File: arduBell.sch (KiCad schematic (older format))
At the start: 20 parts, among them J1 AVR-ISP-6, J2 UART, J3 VCC, J4 BELL, J5 RELAY1, J6 RELAY2, U1 ATMEGA328P-AU, U2 NSL-32, Y1 Crystal_GND2

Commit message: rev 1a, XO fixed, more labels and rearranging
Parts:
- removed Y1: Crystal_GND2, Crystal:Crystal_HC49-4H_Vertical, symbol Device:Crystal_GND2
- added C10, C9: 10p, Capacitor_SMD:C_0603_1608Metric, symbol Device:C_Small
- added Y1: Crystal, symbol Device:Crystal
- C1, C2, C5: value C_Small -> 100n
- C3: value C_Small -> 1u
- C4, C6: value CP_Small -> 4.7u
- J2: symbol dk_Rectangular-Connectors-Headers-Male-Pins:640456-3 -> arduBell-rescue:640456-3-dk_Rectangular-Connectors-Headers-Male-Pins
- J3, J4, J5, J6: symbol dk_Rectangular-Connectors-Headers-Male-Pins:22-23-2021 -> arduBell-rescue:22-23-2021-dk_Rectangular-Connectors-Headers-Male-Pins
- R1, R2, R3: value R_Small -> 1K
- S1: symbol dk_Pushbutton-Switches:GPTS203211B -> arduBell-rescue:GPTS203211B-dk_Pushbutton-Switches
- U1: symbol dk_Embedded-Microcontrollers:ATMEGA328P-AU -> arduBell-rescue:ATMEGA328P-AU-dk_Embedded-Microcontrollers
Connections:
- net GND: now also C10.2, C9.2
- net at U1.7 (PB6): now also C9.1, Y1.1
- net at U1.8 (PB7): now also C10.1, Y1.2
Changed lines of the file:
@@
 $EndDescr
 $Comp
-L dk_Embedded-Microcontrollers:ATMEGA328P-AU U1
+L arduBell-rescue:ATMEGA328P-AU-dk_Embedded-Microcontrollers U1
 U 1 1 5FF53399
 P 5900 3950
@@
 $EndComp
 $Comp
-L dk_Rectangular-Connectors-Headers-Male-Pins:22-23-2021 J3
+L arduBell-rescue:22-23-2021-dk_Rectangular-Connectors-Headers-Male-Pins J3
 U 1 1 5FF54EE3
 P 6750 1700
@@
 P 6050 1250
 F 0 "C2" V 5821 1250 50  0000 C CNN
-F 1 "C_Small" V 5912 1250 50  0000 C CNN
+F 1 "100n" V 5912 1250 50  0000 C CNN
 F 2 "Capacitor_SMD:C_0603_1608Metric" H 6050 1250 50  0001 C CNN
 F 3 "~" H 6050 1250 50  0001 C CNN
@@
 P 6050 1600
 F 0 "C3" V 5821 1600 50  0000 C CNN
-F 1 "C_Small" V 5912 1600 50  0000 C CNN
+F 1 "1u" V 5912 1600 50  0000 C CNN
 F 2 "Capacitor_SMD:C_0603_1608Metric" H 6050 1600 50  0001 C CNN
 F 3 "~" H 6050 1600 50  0001 C CNN
@@
 P 6050 1950
 F 0 "C4" V 5825 1950 50  0000 C CNN
-F 1 "CP_Small" V 5916 1950 50  0000 C CNN
+F 1 "4.7u" V 5916 1950 50  0000 C CNN
 F 2 "Capacitor_SMD:C_1206_3216Metric" H 6050 1950 50  0001 C CNN
 F 3 "~" H 6050 1950 50  0001 C CNN
@@
 Wire Wire Line
 	6600 1700 6650 1700
-$Comp
-L Device:Crystal_GND2 Y1
-U 1 1 5FF6D2C8
-P 4400 2900
-F 0 "Y1" V 4354 3030 50  0000 L CNN
-F 1 "Crystal_GND2" V 4445 3030 50  0000 L CNN
-F 2 "Crystal:Crystal_HC49-4H_Vertical" H 4400 2900 50  0001 C CNN
-F 3 "~" H 4400 2900 50  0001 C CNN
-	1    4400 2900
-	0    1    1    0
-$EndComp
 Wire Wire Line
 	4400 2750 5200 2750
@@
 L power:GND #PWR0105
 U 1 1 5FF6EA88
-P 4100 3000
-F 0 "#PWR0105" H 4100 2750 50  0001 C CNN
-F 1 "GND" H 4105 2827 50  0000 C CNN
-F 2 "" H 4100 3000 50  0001 C CNN
-F 3 "" H 4100 3000 50  0001 C CNN
-	1    4100 3000
-	1    0    0    -1
-$EndComp
-Wire Wire Line
-	4100 3000 4100 2900
-Wire Wire Line
-	4100 2900 4200 2900
+P 3950 2950
+F 0 "#PWR0105" H 3950 2700 50  0001 C CNN
+F 1 "GND" H 3955 2777 50  0000 C CNN
+F 2 "" H 3950 2950 50  0001 C CNN
+F 3 "" H 3950 2950 50  0001 C CNN
+	1    3950 2950
+	1    0    0    -1
+$EndComp
 $Comp
 L Device:C_Small C1
@@
 P 4600 5050
 F 0 "C1" V 4371 5050 50  0000 C CNN
-F 1 "C_Small" V 4462 5050 50  0000 C CNN
+F 1 "100n" V 4462 5050 50  0000 C CNN
 F 2 "Capacitor_SMD:C_0603_1608Metric" H 4600 5050 50  0001 C CNN
 F 3 "~" H 4600 5050 50  0001 C CNN
@@
 P 3850 4750
 F 0 "R2" V 4046 4750 50  0000 C CNN
-F 1 "R_Small" V 3955 4750 50  0000 C CNN
+F 1 "1K" V 3955 4750 50  0000 C CNN
 F 2 "Resistor_SMD:R_0603_1608Metric" H 3850 4750 50  0001 C CNN
 F 3 "~" H 3850 4750 50  0001 C CNN
@@
 P 4150 4650
 F 0 "R3" V 4346 4650 50  0000 C CNN
-F 1 "R_Small" V 4255 4650 50  0000 C CNN
+F 1 "1K" V 4255 4650 50  0000 C CNN
 F 2 "Resistor_SMD:R_0603_1608Metric" H 4150 4650 50  0001 C CNN
 F 3 "~" H 4150 4650 50  0001 C CNN
@@
 	5400 4550 4950 4550
 $Comp
-L dk_Pushbutton-Switches:GPTS203211B S1
+L arduBell-rescue:GPTS203211B-dk_Pushbutton-Switches S1
 U 1 1 5FF7A8EF
 P 1700 4500
@@
 P 1900 3950
 F 0 "R1" H 1959 3996 50  0000 L CNN
-F 1 "R_Small" H 1959 3905 50  0000 L CNN
+F 1 "1K" H 1959 3905 50  0000 L CNN
 F 2 "Resistor_SMD:R_0603_1608Metric" H 1900 3950 50  0001 C CNN
 F 3 "~" H 1900 3950 50  0001 C CNN
@@
 $EndComp
 $Comp
-L dk_Rectangular-Connectors-Headers-Male-Pins:22-23-2021 J4
+L arduBell-rescue:22-23-2021-dk_Rectangular-Connectors-Headers-Male-Pins J4
 U 1 1 6000BCD1
 P 900 5600
@@
 P 2050 5850
 F 0 "C5" H 1958 5804 50  0000 R CNN
-F 1 "C_Small" H 1958 5895 50  0000 R CNN
+F 1 "100n" H 1958 5895 50  0000 R CNN
 F 2 "Capacitor_SMD:C_0603_1608Metric" H 2050 5850 50  0001 C CNN
 F 3 "~" H 2050 5850 50  0001 C CNN
@@
 P 2550 5850
 F 0 "C6" H 2638 5896 50  0000 L CNN
-F 1 "CP_Small" H 2638 5805 50  0000 L CNN
+F 1 "4.7u" H 2638 5805 50  0000 L CNN
 F 2 "Capacitor_SMD:C_1206_3216Metric" H 2550 5850 50  0001 C CNN
 F 3 "~" H 2550 5850 50  0001 C CNN
@@
 Relay2_coil
 $Comp
-L dk_Rectangular-Connectors-Headers-Male-Pins:22-23-2021 J5
+L arduBell-rescue:22-23-2021-dk_Rectangular-Connectors-Headers-Male-Pins J5
 U 1 1 6044A086
 P 3750 950
@@
 	3300 850  3650 850
 $Comp
-L dk_Rectangular-Connectors-Headers-Male-Pins:22-23-2021 J6
+L arduBell-rescue:22-23-2021-dk_Rectangular-Connectors-Headers-Male-Pins J6
 U 1 1 6044D3F4
 P 3750 1550
@@
 	4900 4250 5400 4250
 $Comp
-L dk_Rectangular-Connectors-Headers-Male-Pins:640456-3 J2
+L arduBell-rescue:640456-3-dk_Rectangular-Connectors-Headers-Male-Pins J2
 U 1 1 5FF945AB
 P 3300 4650
@@
 	0    1    1    0
 $EndComp
+$Comp
+L Device:Crystal Y1
+U 1 1 60971625
+P 4400 2900
+F 0 "Y1" V 4354 3031 50  0000 L CNN
+F 1 "Crystal" V 4445 3031 50  0000 L CNN
+F 2 "" H 4400 2900 50  0001 C CNN
+F 3 "~" H 4400 2900 50  0001 C CNN
+	1    4400 2900
+	0    1    1    0
+$EndComp
+$Comp
+L Device:C_Small C9
+U 1 1 6098B825
+P 4250 2750
+F 0 "C9" V 4021 2750 50  0000 C CNN
+F 1 "10p" V 4112 2750 50  0000 C CNN
+F 2 "Capacitor_SMD:C_0603_1608Metric" H 4250 2750 50  0001 C CNN
+F 3 "~" H 4250 2750 50  0001 C CNN
+	1    4250 2750
+	0    1    1    0
+$EndComp
+Wire Wire Line
+	4350 2750 4400 2750
+Connection ~ 4400 2750
+$Comp
+L Device:C_Small C10
+U 1 1 6098F24F
+P 4250 3050
+F 0 "C10" V 4021 3050 50  0000 C CNN
+F 1 "10p" V 4112 3050 50  0000 C CNN
+F 2 "Capacitor_SMD:C_0603_1608Metric" H 4250 3050 50  0001 C CNN
+F 3 "~" H 4250 3050 50  0001 C CNN
+	1    4250 3050
+	0    1    -1   0
+$EndComp
+Wire Wire Line
+	4350 3050 4400 3050
+Connection ~ 4400 3050
+Wire Wire Line
+	4150 2750 4050 2750
+Wire Wire Line
+	4050 2750 4050 2900
+Wire Wire Line
+	4050 3050 4150 3050
+Wire Wire Line
+	4050 2900 3950 2900
+Wire Wire Line
+	3950 2900 3950 2950
+Connection ~ 4050 2900
+Wire Wire Line
+	4050 2900 4050 3050
 $EndSCHEMATC

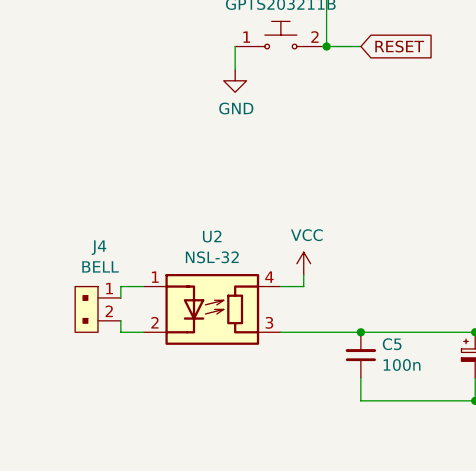
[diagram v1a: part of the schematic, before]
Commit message: rev 1a: optocoupler works, quarz works
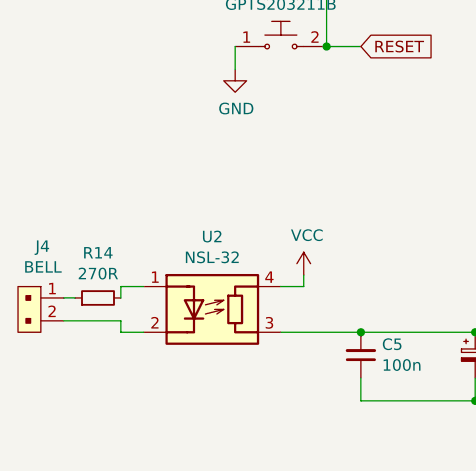
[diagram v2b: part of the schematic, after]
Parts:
- added R14: 270R, Resistor_SMD:R_0603_1608Metric, symbol Device:R_Small
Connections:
- net at U2.1 (A): now also R14.2; no longer J4.1
- new net: J4.1, R14.1
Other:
- moved on the sheet: J4
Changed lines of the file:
@@
 L arduBell-rescue:22-23-2021-dk_Rectangular-Connectors-Headers-Male-Pins J4
 U 1 1 6000BCD1
-P 900 5600
-F 0 "J4" V 675 5608 50  0000 C CNN
-F 1 "BELL" V 766 5608 50  0000 C CNN
-F 2 "digikey-footprints:PinHeader_1x2_P2.54mm_Drill1.02mm" H 1100 5800 60  0001 L CNN
-F 3 "https://media.digikey.com/pdf/Data%20Sheets/Molex%20PDFs/A-6373-N_Series_Dwg_2010-12-03.pdf" H 1100 5900 60  0001 L CNN
-F 4 "WM4200-ND" H 1100 6000 60  0001 L CNN "Digi-Key_PN"
-F 5 "22-23-2021" H 1100 6100 60  0001 L CNN "MPN"
-F 6 "Connectors, Interconnects" H 1100 6200 60  0001 L CNN "Category"
-F 7 "Rectangular Connectors - Headers, Male Pins" H 1100 6300 60  0001 L CNN "Family"
-F 8 "https://media.digikey.com/pdf/Data%20Sheets/Molex%20PDFs/A-6373-N_Series_Dwg_2010-12-03.pdf" H 1100 6400 60  0001 L CNN "DK_Datasheet_Link"
-F 9 "/product-detail/en/molex/22-23-2021/WM4200-ND/26667" H 1100 6500 60  0001 L CNN "DK_Detail_Page"
-F 10 "CONN HEADER VERT 2POS 2.54MM" H 1100 6600 60  0001 L CNN "Description"
-F 11 "Molex" H 1100 6700 60  0001 L CNN "Manufacturer"
-F 12 "Active" H 1100 6800 60  0001 L CNN "Status"
-	1    900  5600
+P 650 5600
+F 0 "J4" V 425 5608 50  0000 C CNN
+F 1 "BELL" V 516 5608 50  0000 C CNN
+F 2 "digikey-footprints:PinHeader_1x2_P2.54mm_Drill1.02mm" H 850 5800 60  0001 L CNN
+F 3 "https://media.digikey.com/pdf/Data%20Sheets/Molex%20PDFs/A-6373-N_Series_Dwg_2010-12-03.pdf" H 850 5900 60  0001 L CNN
+F 4 "WM4200-ND" H 850 6000 60  0001 L CNN "Digi-Key_PN"
+F 5 "22-23-2021" H 850 6100 60  0001 L CNN "MPN"
+F 6 "Connectors, Interconnects" H 850 6200 60  0001 L CNN "Category"
+F 7 "Rectangular Connectors - Headers, Male Pins" H 850 6300 60  0001 L CNN "Family"
+F 8 "https://media.digikey.com/pdf/Data%20Sheets/Molex%20PDFs/A-6373-N_Series_Dwg_2010-12-03.pdf" H 850 6400 60  0001 L CNN "DK_Datasheet_Link"
+F 9 "/product-detail/en/molex/22-23-2021/WM4200-ND/26667" H 850 6500 60  0001 L CNN "DK_Detail_Page"
+F 10 "CONN HEADER VERT 2POS 2.54MM" H 850 6600 60  0001 L CNN "Description"
+F 11 "Molex" H 850 6700 60  0001 L CNN "Manufacturer"
+F 12 "Active" H 850 6800 60  0001 L CNN "Status"
+	1    650  5600
 	0    1    1    0
 $EndComp
@@
 Wire Wire Line
 	4050 2900 4050 3050
+$Comp
+L Device:R_Small R14
+U 1 1 611CCF5C
+P 900 5600
+F 0 "R14" V 1096 5600 50  0000 C CNN
+F 1 "270R" V 1005 5600 50  0000 C CNN
+F 2 "Resistor_SMD:R_0603_1608Metric" H 900 5600 50  0001 C CNN
+F 3 "~" H 900 5600 50  0001 C CNN
+	1    900  5600
+	0    -1   -1   0
+$EndComp
+Wire Wire Line
+	750  5600 800  5600
+Wire Wire Line
+	750  5700 1000 5700
 $EndSCHEMATC
